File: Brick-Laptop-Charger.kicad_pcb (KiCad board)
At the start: 2 copper layers, 78.7 x 61 mm, 50 parts, among them P1 TST, P10 Power Out, P2 TST, P3 TST, P4 TST, P5 TST, P6 TST, P7 TST, P8 Battery 1, P9 Battery 2, U1 LM5117*PM*

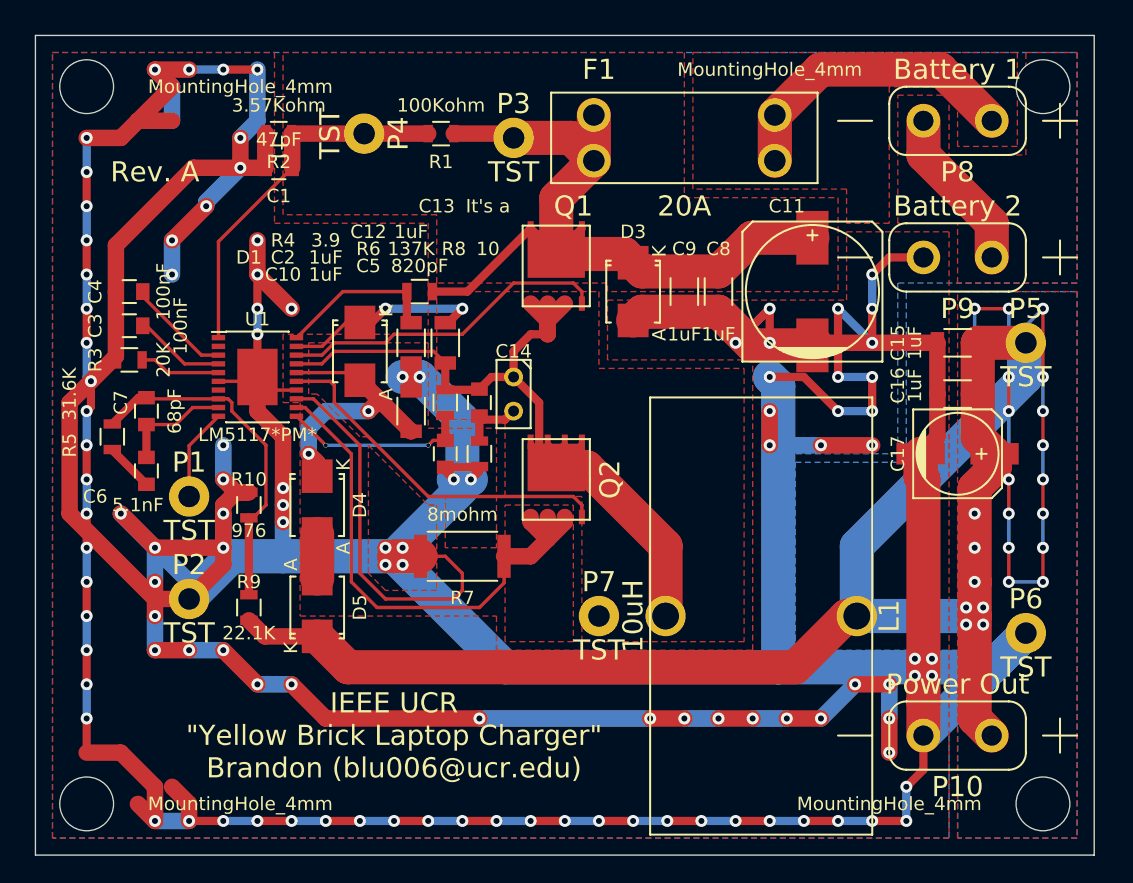
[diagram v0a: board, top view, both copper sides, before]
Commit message: Separated analog and power grounds.  Most of power current now flows through a separate path from analog circuitry (see exposed trace on bottom of PCB).  Reduced capacitive coupling between ground planes and MOSFET switches.  Smoothed copper pours.  Added power in LED.
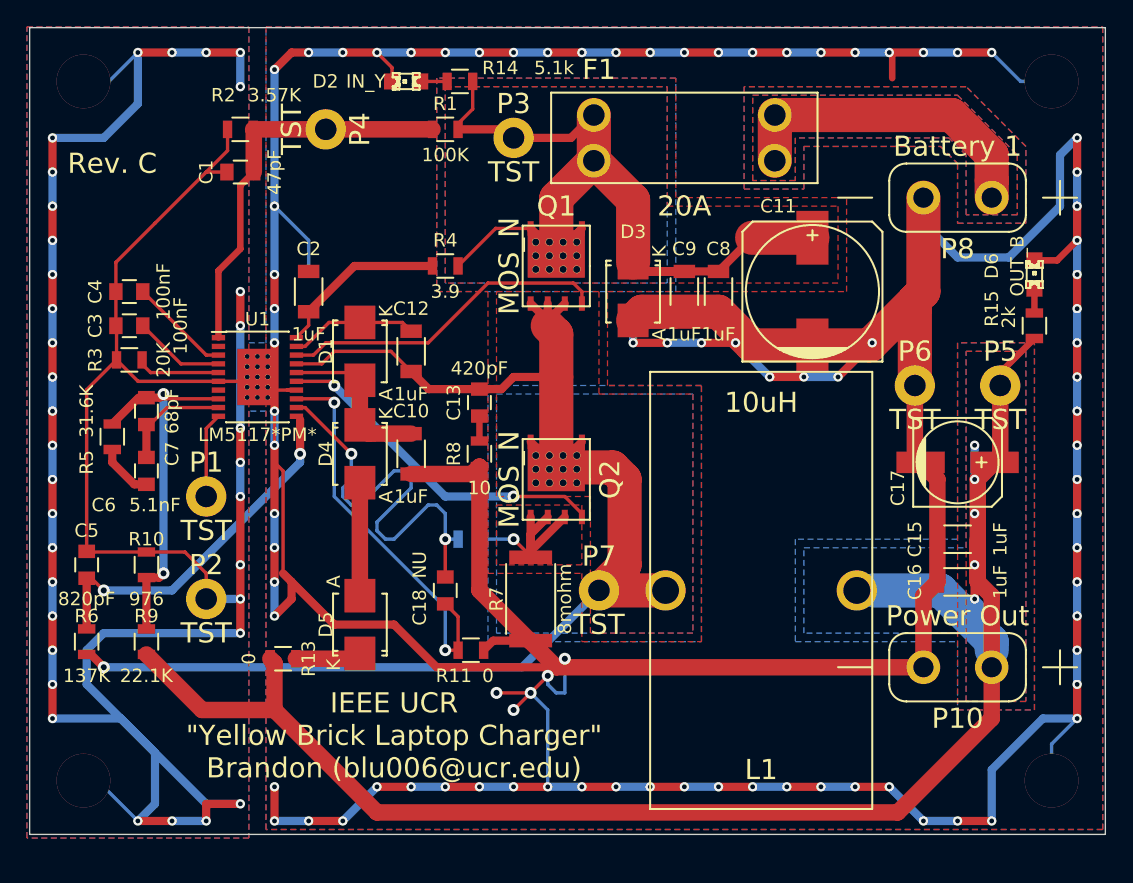
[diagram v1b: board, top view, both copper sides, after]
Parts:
- removed C14: Mystery, Discret:C1
- removed MountingHole_4mm (x4): VAL**, Mounting_Holes:MountingHole_4mm
- removed P9: Battery 2, This:BIG_CONN
- added ?: Val**, Mounting_Holes:MountingHole_4mm, F.Cu at (142.0, 72.0)
- added ?: VAL**, Mounting_Holes:MountingHole_4mm, F.Cu at (142.0, 124.0)
- added ?: VAL**, Mounting_Holes:MountingHole_4mm, F.Cu at (214.0, 124.0)
- added ?: VAL**, Mounting_Holes:MountingHole_4mm, F.Cu at (214.0, 72.0)
- added C18: NU, Capacitors_SMD:C_0805, F.Cu at (168.9, 109.9)
- added D2: IN_Y, LEDs:LED-0805, F.Cu at (166.0, 72.0)
- added D6: OUT_B, LEDs:LED-0805, F.Cu at (212.7, 86.4)
- added R11: 0, Resistors_SMD:R_0805, F.Cu at (170.8, 114.3)
- added R12: 0, Resistors_SMD:R_0805, B.Cu at (170.8, 106.0)
- added R13: 0, Resistors_SMD:R_0805, F.Cu at (156.8, 114.9)
- added R14: 5.1k, Resistors_SMD:R_0805, F.Cu at (170.0, 72.0)
- added R15: 2k, Resistors_SMD:R_0805, F.Cu at (212.7, 90.2)
- C13: value It's a -> 420pF
- Q1, Q2: value (none) -> MOS_N
- R1: value 100Kohm -> 100K
- R2: value 3.57Kohm -> 3.57K
- moved R6 32.1 mm to (142.2, 113.7), turned to 90 degrees
- moved C5 27.9 mm to (142.2, 108.0), turned to 90 degrees
- moved P6 20.2 mm to (203.8, 94.6)
- moved C15 14.6 mm to (207.0, 106.0)
- moved C16 14.0 mm to (207.0, 109.2)
- moved R10 8.82 mm to (146.7, 108.0)
- moved C2 8.52 mm to (158.8, 87.6), turned to 90 degrees
- moved R9 8.03 mm to (146.7, 113.7)
- moved R7 5.99 mm to (175.3, 110.5), turned to 270 degrees
- moved P8 5.71 mm to (207.0, 80.6)
- moved P10 5.08 mm to (207.0, 115.6)
- moved D4 4.96 mm to (162.6, 99.7)
- moved P5 3.70 mm to (210.2, 94.6)
- moved D5 3.42 mm to (162.6, 112.4)
- moved C10 3.17 mm to (166.4, 99.7), turned to 270 degrees
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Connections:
- net Net-(C11-Pad1) renamed /POWER
- C1 pad 2: GND -> GNDA
- C10 pad 2: GND -> GNDA
- C11 pad 2: GND -> GNDA
- C15 pad 2: GND -> GNDA
- C16 pad 2: GND -> GNDA
- C17 pad 2: GND -> GNDA
- C2 pad 2: GND -> GNDA
- C3 pad 2: GND -> GNDA
- C4 pad 2: GND -> GNDA
- C5 pad 2: GND -> GNDA
- C8 pad 2: GND -> GNDA
- C9 pad 2: GND -> GNDA
- D3 pad 1: GND -> GNDA
- D5 pad 2: +19V -> Net-(D5-Pad2)
- P10 pad 1: GND -> GNDA
- P2 pad 1: GND -> GNDA
- P6 pad 1: GND -> GNDA
- P8 pad 1: Net-(P8-Pad1) -> GNDA
- R10 pad 2: GND -> GNDA
- R2 pad 2: GND -> GNDA
- R3 pad 2: GND -> GNDA
- R7 pad 2: GND -> GNDA
- R8 pad 2: GND -> GNDA
- U1 pad 12: Net-(Q2-PadS) -> Net-(C18-Pad1)
- U1 pad 13: GND -> Net-(C18-Pad2)
- U1 pad 14: GND -> GNDA
- U1 pad 6: GND -> GNDA
- U1 pad EP: GND -> GNDA
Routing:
- net GNDA: track 0.00 -> 677.4 mm, vias 0 -> 121
- net GND: track 647.0 -> 0.00 mm, vias 111 -> 0
- net +19V: track 194.5 -> 137.5 mm, vias 23 -> 5
- net Net-(C12-Pad1): track 65.4 -> 106.1 mm, vias 0 -> 1
- net Net-(C18-Pad1): track 0.00 -> 32.8 mm, vias 0 -> 2
- net Net-(C18-Pad2): track 0.00 -> 29.6 mm, vias 0 -> 2
- net Net-(Q2-PadS): track 39.7 -> 15.2 mm, vias 0 -> 1
- net Net-(C5-Pad1): track 14.5 -> 27.5 mm
- net Net-(P8-Pad1): track 12.3 -> 0.00 mm
- net Net-(C10-Pad1): track 21.0 -> 12.4 mm, vias 2 -> 0
- net Net-(C12-Pad2): track 15.2 -> 9.54 mm, vias 2 -> 0
- net Net-(D4-Pad1): track 3.32 -> 8.40 mm
- net Net-(D5-Pad2): track 0.00 -> 4.93 mm
- net /POWER: track 65.2 -> 69.1 mm
- net Net-(C13-Pad2): track 4.77 -> 1.86 mm
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- added copper zone on B.Cu, net +BATT
- added copper zone on B.Cu, net /POWER
- added copper zone on B.Cu, net GNDA
- added copper zone on F.Cu, net GNDA
- added copper zone on B.Cu, net Net-(C12-Pad1)
- removed copper zone on B.Cu, net GND
- removed copper zone on F.Cu, net GND
- removed copper zone on F.Cu, net Net-(P8-Pad1)
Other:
- board size 78.7 x 61 mm -> 80 x 60 mm
- board text added: "Rev. C"
- board text removed: "Rev. A"
